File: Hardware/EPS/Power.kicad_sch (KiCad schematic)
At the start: 20 parts, among them U501 TPS27081ADDCR, U502 RT8258GE, U503 B230A-13-F

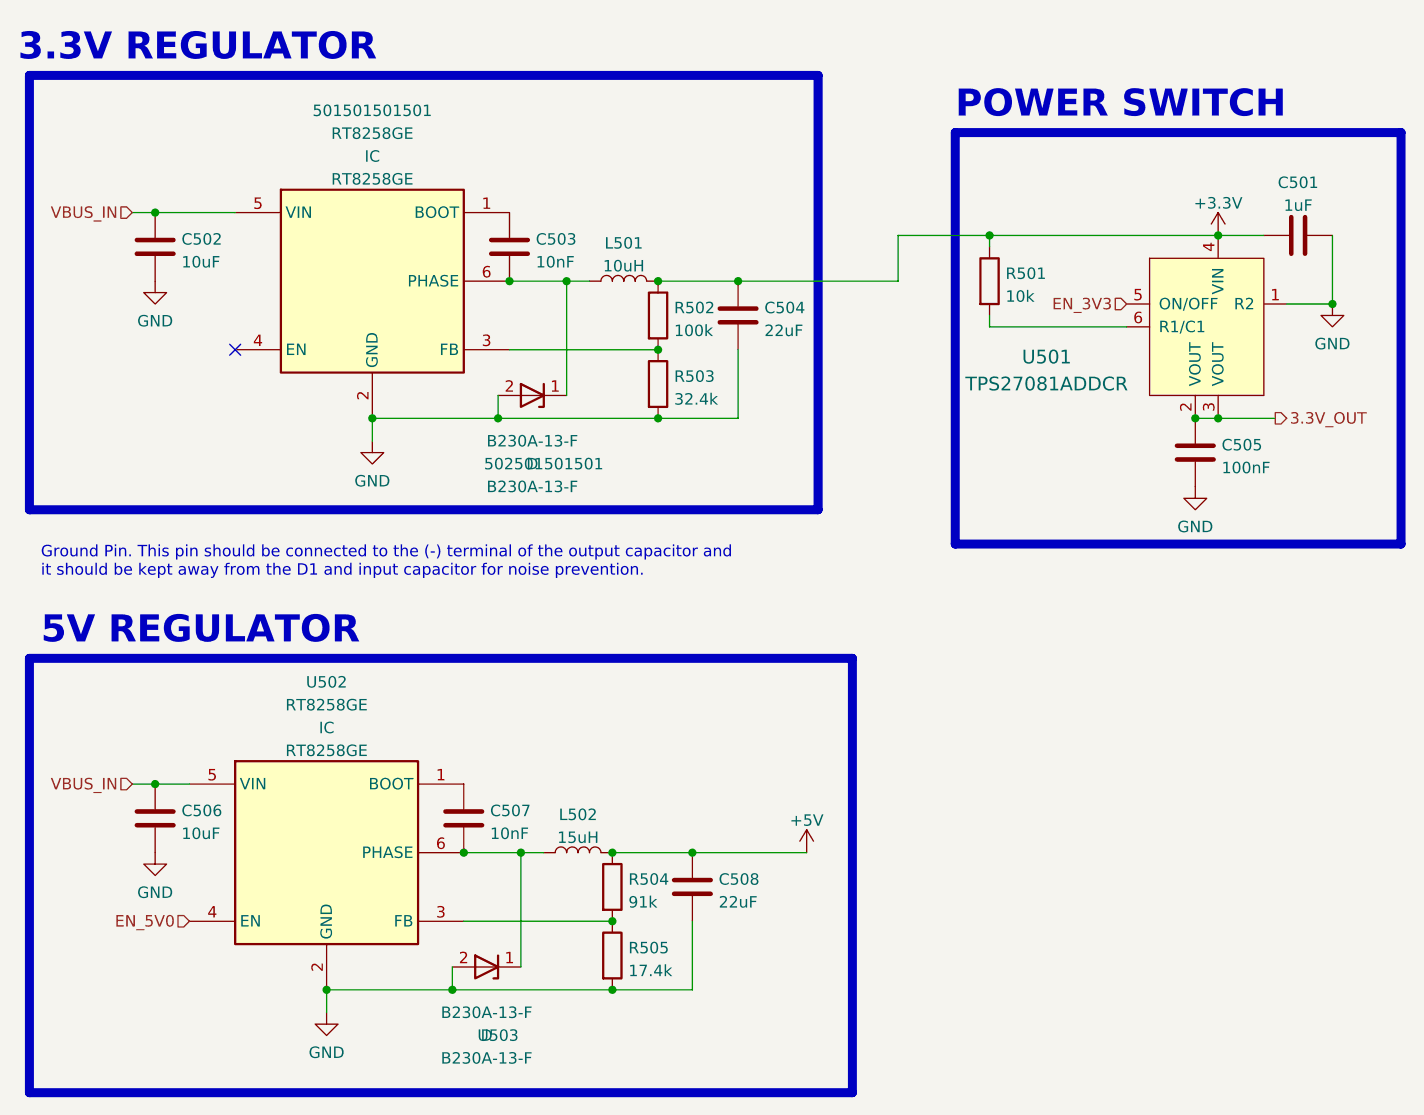
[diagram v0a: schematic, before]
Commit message: Changed uC pinout and finished uC routing
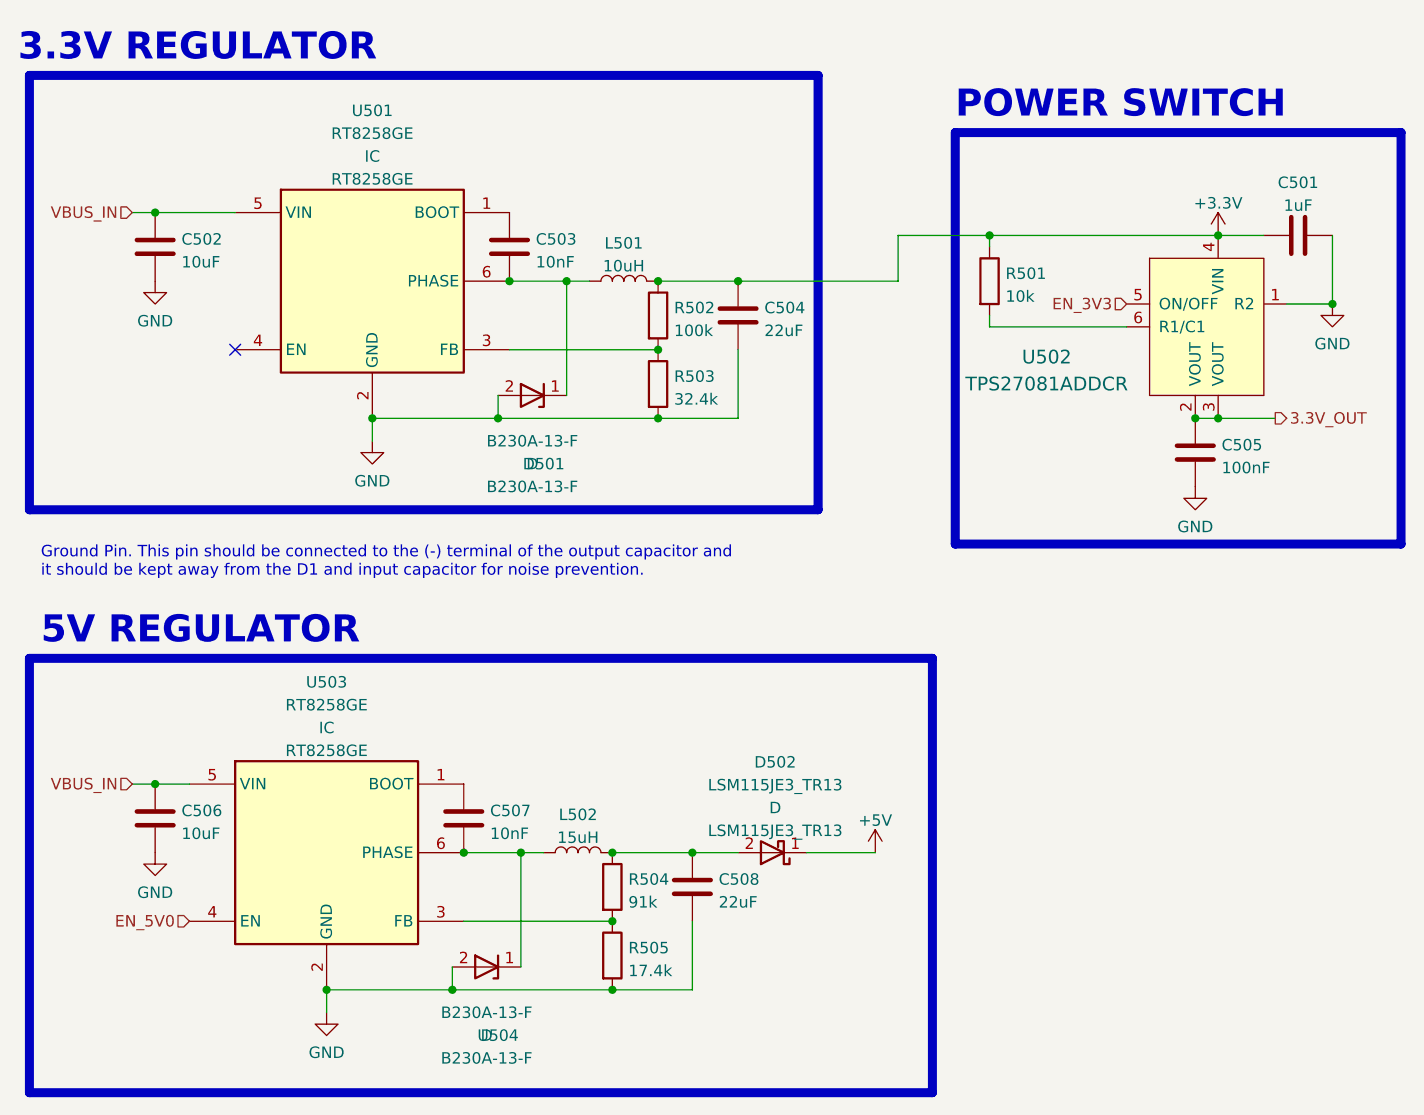
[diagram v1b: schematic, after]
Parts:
- added D502: LSM115JE3_TR13, LSM115JE3_TR13:DIOM5436X330N, symbol LSM115JE3_TR13:LSM115JE3_TR13
- renumbered 502501501501 to D501, 501501501501 to U501, U501 to U502, U502 to U503, U503 to U504
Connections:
- net +5V: now also D502.1 (K); no longer C508.1, L502.2, R504.1
- new net: C508.1, D502.2 (A), L502.2, R504.1
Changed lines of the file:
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@@
   )
   (no_connect (at 116.84 77.47))
-  (polyline (pts (xy 185.42 160.02) (xy 93.98 160.02))
+  (polyline (pts (xy 194.31 160.02) (xy 93.98 160.02))
     (stroke (width 1) (type default) (color 0 0 0 0))
   )
-  (polyline (pts (xy 93.98 111.76) (xy 185.42 111.76))
+  (polyline (pts (xy 93.98 111.76) (xy 194.31 111.76))
     (stroke (width 1) (type default) (color 0 0 0 0))
   )
@@
     (stroke (width 1) (type default) (color 0 0 0 0))
   )
-  (wire (pts (xy 167.64 133.35) (xy 180.34 133.35))
+  (wire (pts (xy 167.64 133.35) (xy 172.72 133.35))
     (stroke (width 0) (type default) (color 0 0 0 0))
   )
@@
     (stroke (width 0) (type default) (color 0 0 0 0))
   )
+  (wire (pts (xy 180.34 133.35) (xy 187.96 133.35))
+    (stroke (width 0) (type default) (color 0 0 0 0))
+  )
   (wire (pts (xy 142.24 133.35) (xy 148.59 133.35))
     (stroke (width 0) (type default) (color 0 0 0 0))
@@
     (stroke (width 1) (type default) (color 0 0 0 0))
   )
-  (polyline (pts (xy 185.42 111.76) (xy 185.42 160.02))
+  (polyline (pts (xy 194.31 111.76) (xy 194.31 160.02))
     (stroke (width 1) (type default) (color 0 0 0 0))
   )
@@
   (symbol (lib_id "dk_PMIC-Power-Distribution-Switches-Load-Drivers:TPS27081ADDCR") (at 223.52 72.39 0) (unit 1)
     (in_bom yes) (on_board yes)
-    (property "Reference" "U501" (id 0) (at 207.01 78.2866 0)
+    (property "Reference" "U502" (id 0) (at 207.01 78.2866 0)
       (effects (font (size 1.524 1.524)))
     )
@@
   (symbol (lib_id "B230A-13-F:B230A-13-F") (at 149.86 82.55 180) (unit 1)
     (in_bom yes) (on_board yes)
-    (property "Reference" "502501501501" (id 0) (at 151.13 90.17 0))
+    (property "Reference" "D501" (id 0) (at 151.13 90.17 0))
     (property "Value" "B230A-13-F" (id 1) (at 149.86 87.63 0))
     (property "Footprint" "B230A-13-F:DIOM5226X230N" (id 2) (at 149.86 82.55 0)
@@
   (symbol (lib_id "RT8258GE:RT8258GE") (at 111.76 125.73 0) (unit 1)
     (in_bom yes) (on_board yes) (fields_autoplaced)
-    (property "Reference" "U502" (id 0) (at 127 114.4164 0))
+    (property "Reference" "U503" (id 0) (at 127 114.4164 0))
     (property "Value" "RT8258GE" (id 1) (at 127 116.9533 0))
     (property "Footprint" "RT8258GE:SOT94P279X130-6N" (id 2) (at 111.76 125.73 0)
@@
   (symbol (lib_id "RT8258GE:RT8258GE") (at 116.84 62.23 0) (unit 1)
     (in_bom yes) (on_board yes) (fields_autoplaced)
-    (property "Reference" "501501501501" (id 0) (at 132.08 50.9164 0))
+    (property "Reference" "U501" (id 0) (at 132.08 50.9164 0))
     (property "Value" "RT8258GE" (id 1) (at 132.08 53.4533 0))
     (property "Footprint" "RT8258GE:SOT94P279X130-6N" (id 2) (at 116.84 62.23 0)
@@
     (pin "2")
   )
+  (symbol (lib_id "LSM115JE3_TR13:LSM115JE3_TR13") (at 176.53 133.35 180) (unit 1)
+    (in_bom yes) (on_board yes) (fields_autoplaced)
+    (property "Reference" "D502" (id 0) (at 176.8475 123.3064 0))
+    (property "Value" "LSM115JE3_TR13" (id 1) (at 176.8475 125.8433 0))
+    (property "Footprint" "LSM115JE3_TR13:DIOM5436X330N" (id 2) (at 176.53 133.35 0)
+      (effects (font (size 1.27 1.27)) hide)
+    )
+    (property "Datasheet" "" (id 3) (at 176.53 133.35 0)
+      (effects (font (size 1.27 1.27)) hide)
+    )
+    (property "Reference_1" "D" (id 4) (at 176.8475 128.3802 0))
+    (property "Value_1" "LSM115JE3_TR13" (id 5) (at 176.8475 130.9171 0))
+    (property "Footprint_1" "DIOM5436X330N" (id 6) (at 163.83 39.7 0)
+      (effects (font (size 1.27 1.27)) (justify left top) hide)
+    )
+    (property "Datasheet_1" "https://media.digikey.com/pdf/Data%20Sheets/Microsemi%20PDFs/LSM115J.pdf" (id 7) (at 163.83 -60.3 0)
+      (effects (font (size 1.27 1.27)) (justify left top) hide)
+    )
+    (property "Height" "3.3" (id 8) (at 163.83 -260.3 0)
+      (effects (font (size 1.27 1.27)) (justify left top) hide)
+    )
+    (property "Manufacturer_Name" "Microsemi Corporation" (id 9) (at 163.83 -360.3 0)
+      (effects (font (size 1.27 1.27)) (justify left top) hide)
+    )
+    (property "Manufacturer_Part_Number" "LSM115JE3/TR13" (id 10) (at 163.83 -460.3 0)
+      (effects (font (size 1.27 1.27)) (justify left top) hide)
+    )
+    (property "Mouser Part Number" "494-LSM115JE3/TR13" (id 11) (at 163.83 -560.3 0)
+      (effects (font (size 1.27 1.27)) (justify left top) hide)
+    )
+    (property "Mouser Price/Stock" "https://www.mouser.co.uk/ProductDetail/Microchip-Microsemi/LSM115JE3-TR13/?qs=6jAvgNDGUA8H9k1qUsKdHA%3D%3D" (id 12) (at 163.83 -660.3 0)
+      (effects (font (size 1.27 1.27)) (justify left top) hide)
+    )
+    (property "Arrow Part Number" "LSM115JE3/TR13" (id 13) (at 163.83 -760.3 0)
+      (effects (font (size 1.27 1.27)) (justify left top) hide)
+    )
+    (property "Arrow Price/Stock" "https://www.arrow.com/en/products/lsm115je3tr13/microsemi" (id 14) (at 163.83 -860.3 0)
+      (effects (font (size 1.27 1.27)) (justify left top) hide)
+    )
+    (pin "1")
+    (pin "2")
+  )
   (symbol (lib_id "Device:C") (at 107.95 129.54 0) (unit 1)
     (in_bom yes) (on_board yes) (fields_autoplaced)
@@
     (pin "1")
   )
-  (symbol (lib_id "power:+5V") (at 180.34 133.35 0) (unit 1)
+  (symbol (lib_id "power:+5V") (at 187.96 133.35 0) (unit 1)
     (in_bom yes) (on_board yes) (fields_autoplaced)
-    (property "Reference" "#PWR0507" (id 0) (at 180.34 137.16 0)
+    (property "Reference" "#PWR0507" (id 0) (at 187.96 137.16 0)
       (effects (font (size 1.27 1.27)) hide)
     )
-    (property "Value" "+5V" (id 1) (at 180.34 129.7742 0))
-    (property "Footprint" "" (id 2) (at 180.34 133.35 0)
+    (property "Value" "+5V" (id 1) (at 187.96 129.7742 0))
+    (property "Footprint" "" (id 2) (at 187.96 133.35 0)
       (effects (font (size 1.27 1.27)) hide)
     )
-    (property "Datasheet" "" (id 3) (at 180.34 133.35 0)
+    (property "Datasheet" "" (id 3) (at 187.96 133.35 0)
       (effects (font (size 1.27 1.27)) hide)
     )
@@
   (symbol (lib_id "B230A-13-F:B230A-13-F") (at 144.78 146.05 180) (unit 1)
     (in_bom yes) (on_board yes)
-    (property "Reference" "U503" (id 0) (at 146.05 153.67 0))
+    (property "Reference" "U504" (id 0) (at 146.05 153.67 0))
     (property "Value" "B230A-13-F" (id 1) (at 144.78 151.13 0))
     (property "Footprint" "B230A-13-F:DIOM5226X230N" (id 2) (at 144.78 146.05 0)

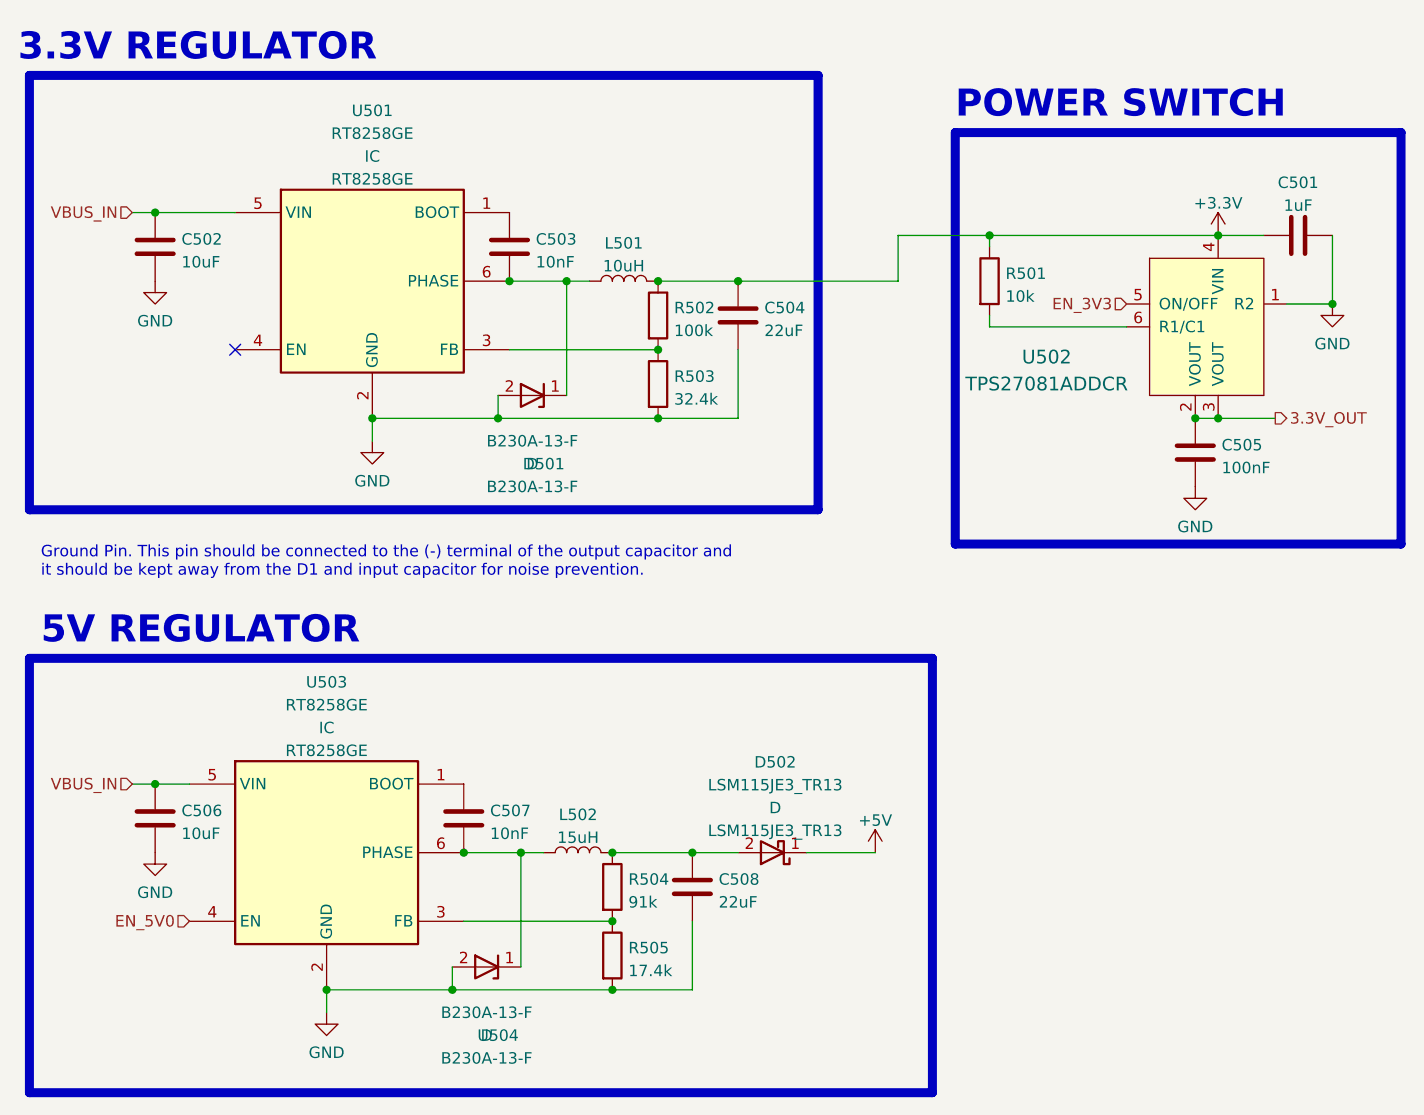
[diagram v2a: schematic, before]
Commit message: Updated to KiCAD 7.0
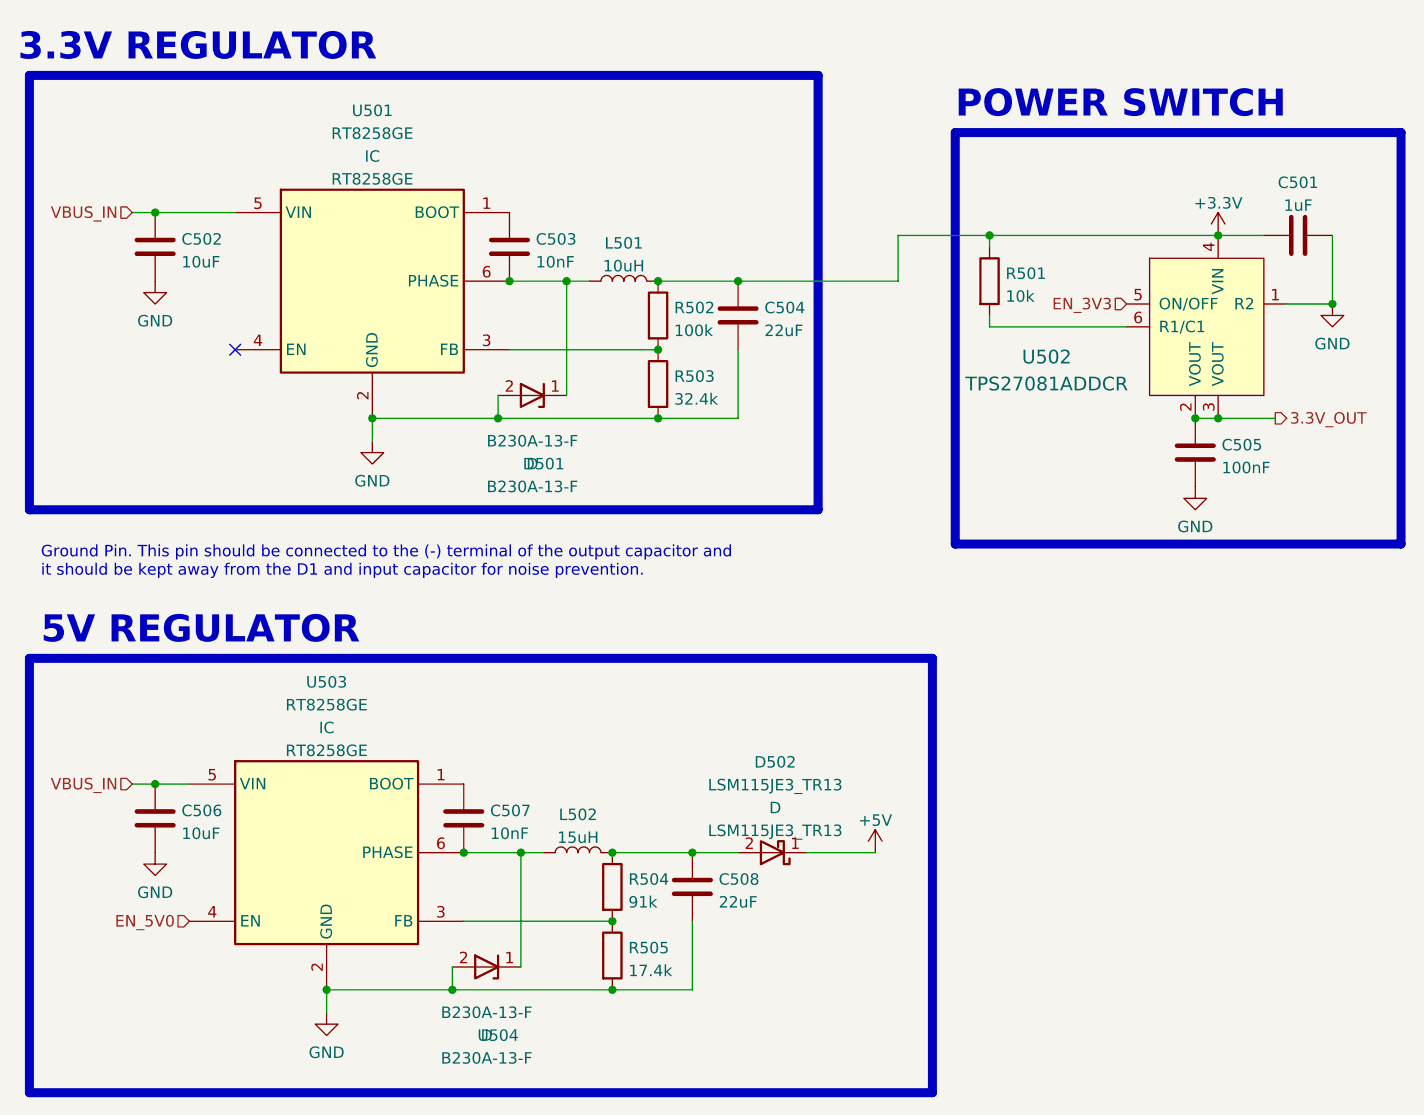
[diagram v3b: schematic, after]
